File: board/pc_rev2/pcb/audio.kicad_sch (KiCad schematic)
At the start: 29 parts, among them J8 GND Pins, J9 Conn_01x05, Q1 2SC1815, Q2 2SA1015, U3 LMV324B

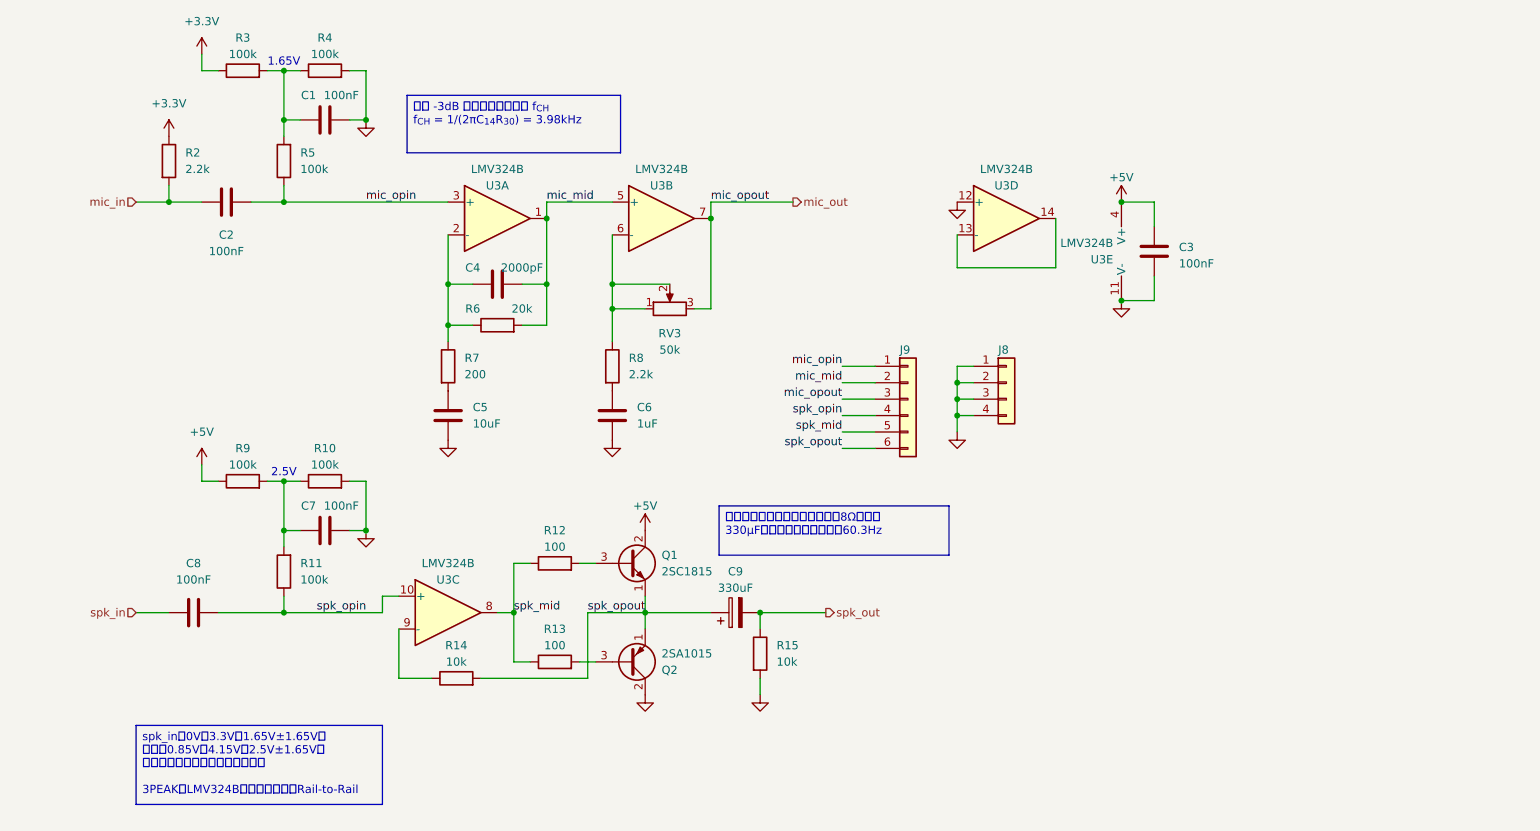
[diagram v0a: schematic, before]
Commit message: MSMP-IFを追加、スピーカ出力をOFFにする仕組みを追加（WIP）
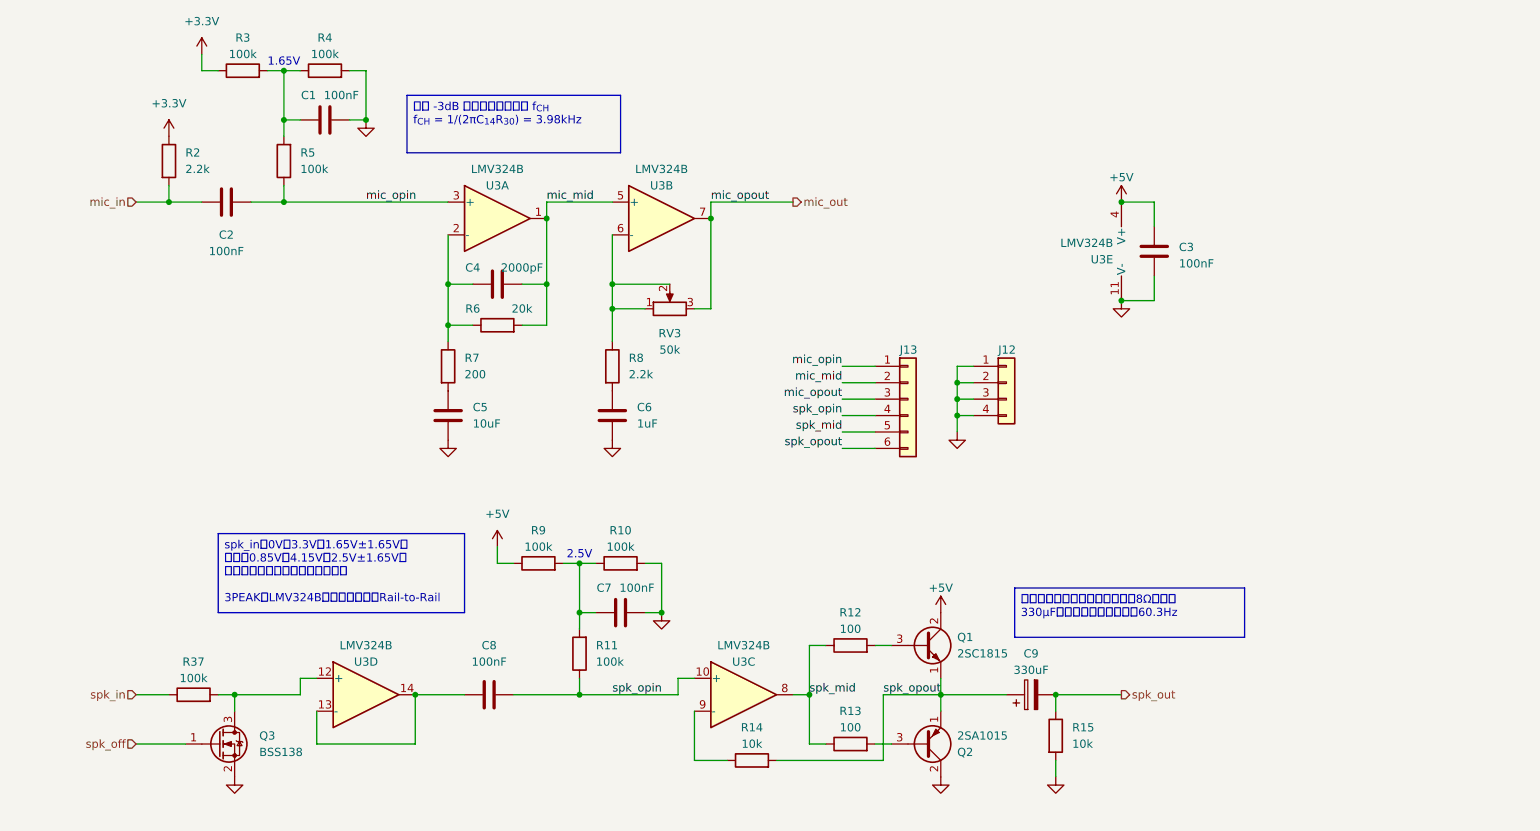
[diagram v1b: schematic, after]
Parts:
- added Q3: BSS138, Package_TO_SOT_SMD:SOT-23_Handsoldering, symbol Device:Q_NMOS_GSD
- added R37: 100k, Resistor_SMD:R_0603_1608Metric_Pad0.98x0.95mm_HandSolder, symbol Device:R
- renumbered J8 to J12, J9 to J13
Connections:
- net GND: now also Q3.2 (S); no longer U3.12 (+)
- net spk_in: now also R37.1; no longer C8.1
- net at U3.13 (-), U3.14: now also C8.1
- new net: Q3.3 (D), R37.2, U3.12 (+)
- new net spk_off: Q3.1 (G)
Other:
- moved on the sheet: C7, C8, C9, Q1, Q2, R10, R11, R12, R13, R14, R15, R9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

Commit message: ADCの8ch化＆スピーカーミュートの仕組み変更
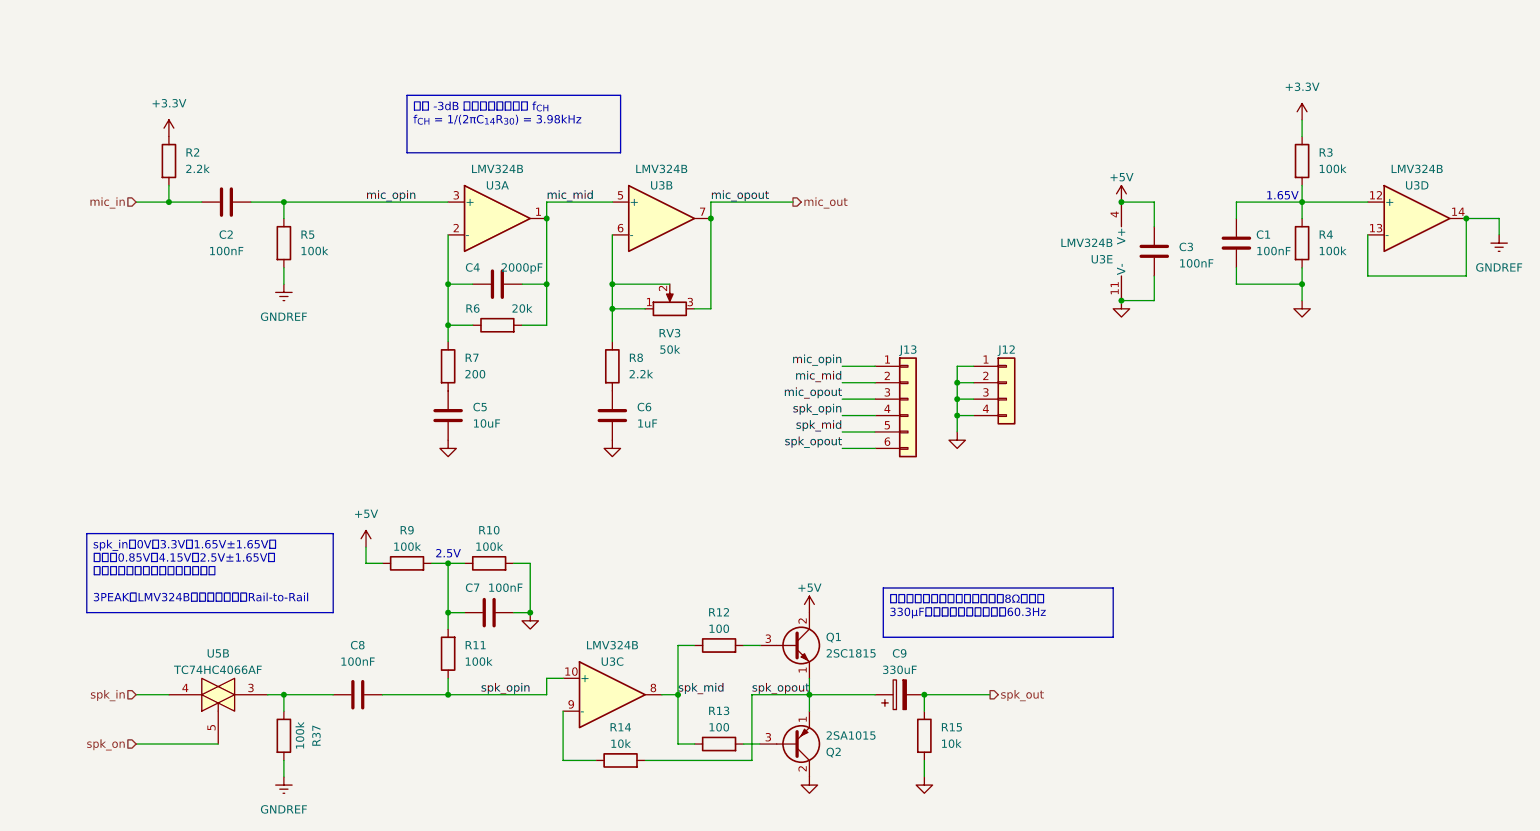
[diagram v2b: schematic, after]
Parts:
- removed Q3: BSS138, Package_TO_SOT_SMD:SOT-23_Handsoldering, symbol Device:Q_NMOS_GSD
- added U5: TC74HC4066AF, Package_SO:SO-14_5.3x10.2mm_P1.27mm, symbol 4xxx:4066
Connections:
- net spk_in: now also U5.4; no longer R37.1
- net at C1.1, R3.2, R4.1: now also U3.12 (+); no longer R5.2
- net GNDREF: now reaches R37.2
- net GNDREF: now also R5.2, U3.13 (-), U3.14; no longer U3.12 (+)
- new net: C8.1, R37.1, U5.3
- new net spk_on: U5.5
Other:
- moved on the sheet: C1, C7, C8, C9, Q1, Q2, R10, R11, R12, R13, R14, R15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

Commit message: 諸々改良＆基板デザイン（WIP）
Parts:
- removed Q1: 2SC1815, Package_TO_SOT_THT:TO-92_Inline, symbol Transistor_BJT:2SC1815
- removed Q2: 2SA1015, Package_TO_SOT_THT:TO-92_Inline, symbol Transistor_BJT:2SA1015
- added C17: 100nF, Capacitor_SMD:C_0603_1608Metric_Pad1.08x0.95mm_HandSolder, symbol Device:C
- added D2: BAT54S, Package_TO_SOT_SMD:SOT-23, symbol Diode:BAT54S
- added J17: GND Pins, Connector_PinHeader_2.54mm:PinHeader_1x02_P2.54mm_Vertical, symbol Connector_Generic:Conn_01x02
- added J18: Conn_01x05, Connector_PinHeader_2.54mm:PinHeader_1x03_P2.54mm_Vertical, symbol Connector_Generic:Conn_01x03
- added J19: Conn_01x02, Connector_PinHeader_2.54mm:PinHeader_1x02_P2.54mm_Vertical, symbol Connector_Generic:Conn_01x02
- added Q1: BC817BPN, Package_TO_SOT_SMD:SOT-457T, symbol Transistor_BJT:Q_Dual_NPN_PNP_E1B1C2E2B2C1
- added R38: 10k, Resistor_SMD:R_0603_1608Metric_Pad0.98x0.95mm_HandSolder, symbol Device:R
- C9: value 330uF -> 470uF; footprint Capacitor_THT:CP_Radial_D6.3mm_P2.50mm -> Capacitor_THT:CP_Radial_D8.0mm_P3.50mm
- J12: footprint Connector_PinHeader_2.54mm:PinHeader_1x04_P2.54mm_Vertical -> Connector_PinHeader_2.54mm:PinHeader_1x02_P2.54mm_Vertical; symbol Connector_Generic:Conn_01x04 -> Connector_Generic:Conn_01x02
- J13: value Conn_01x05 -> Conn_01x02; footprint Connector_PinHeader_2.54mm:PinHeader_1x06_P2.54mm_Vertical -> Connector_PinHeader_2.54mm:PinHeader_1x02_P2.54mm_Vertical; symbol Connector_Generic:Conn_01x06 -> Connector_Generic:Conn_01x02
- R12, R13: value 100 -> 33
- RV3: footprint Potentiometer_SMD:Potentiometer_Bourns_TC33X_Vertical -> uchan:Potentiometer_Suntan_TSR-3386K_Vertical; Manufacturer (none) -> SUNTAN; Manufacturer PN (none) -> TSR-3386K-EY5-503TR
- U3: Manufacturer (none) -> 3PEAK; Manufacturer PN (none) -> LMV324B-TR
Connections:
- net +3.3V: now also D2.2 (K)
- net +5V: now also C17.2, Q1.6 (C1)
- net GND: now also C17.1, D2.1 (A), J17.1 (Pin_1), J17.2 (Pin_2), J19.2 (Pin_2), Q1.3 (C2); no longer J12.3 (Pin_3), J12.4 (Pin_4)
- net GNDREF: now also U3.1, U3.2 (-); no longer U3.13 (-), U3.14
- net mic_mid: now also U3.10 (+), U3.14; no longer U3.1, U3.5 (+)
- net mic_opin: now also U3.12 (+); no longer U3.3 (+)
- net mic_out: now also D2.3 (COM), J19.1 (Pin_1), R38.2; no longer J13.3 (Pin_3), RV3.3, U3.7
- net spk_in: now also U5.1; no longer U5.4
- net spk_mid: now also U3.7, J18.2 (Pin_2); no longer J13.5 (Pin_5), U3.8
- net spk_on: now also U5.13; no longer U5.5
- net spk_opin: now also U3.5 (+), J18.1 (Pin_1); no longer J13.4 (Pin_4), U3.10 (+)
- net spk_opout: now also J18.3 (Pin_3), Q1.1 (E1), Q1.4 (E2); no longer J13.6 (Pin_6)
- net at C4.1, R6.1, R7.1: now also U3.13 (-); no longer U3.2 (-)
- net at C1.1, R3.2, R4.1: now also U3.3 (+); no longer U3.12 (+)
- net at R8.1, RV3.1, RV3.2: now also U3.9 (-); no longer U3.6 (-)
- net at R12.2: now also Q1.2 (B1)
- net at R13.2: now also Q1.5 (B2)
- net at R14.1: now also U3.6 (-); no longer U3.9 (-)
- net at C8.1, R37.1: now also U5.2; no longer U5.3
- new net: R38.1, RV3.3, U3.8

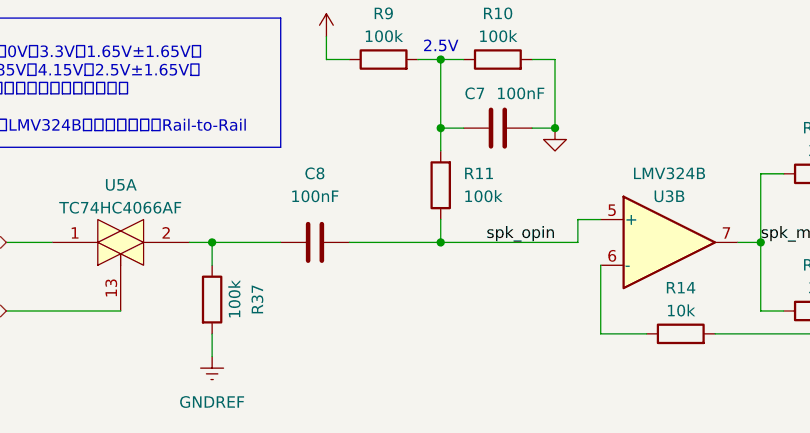
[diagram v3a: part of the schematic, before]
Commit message: ポップノイズ防止用コンデンサ追加＆シルク微修正
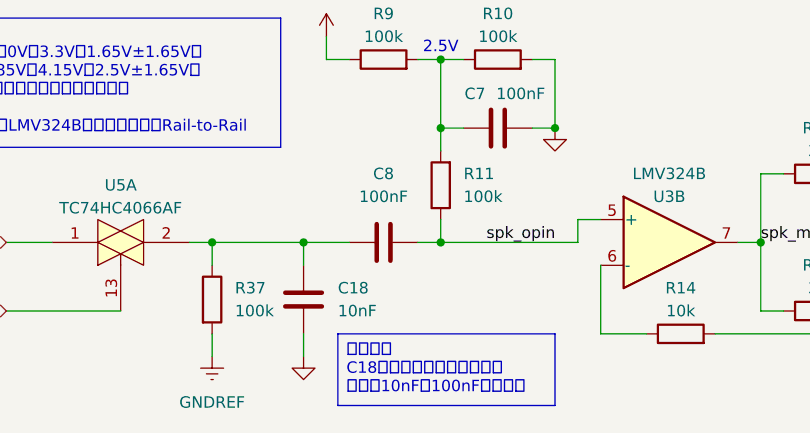
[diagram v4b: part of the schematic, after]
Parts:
- added C18: 10nF, Capacitor_SMD:C_0603_1608Metric_Pad1.08x0.95mm_HandSolder, symbol Device:C
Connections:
- net GND: now also C18.2
- net at C8.1, R37.1, U5.2: now also C18.1
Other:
- moved on the sheet: C8

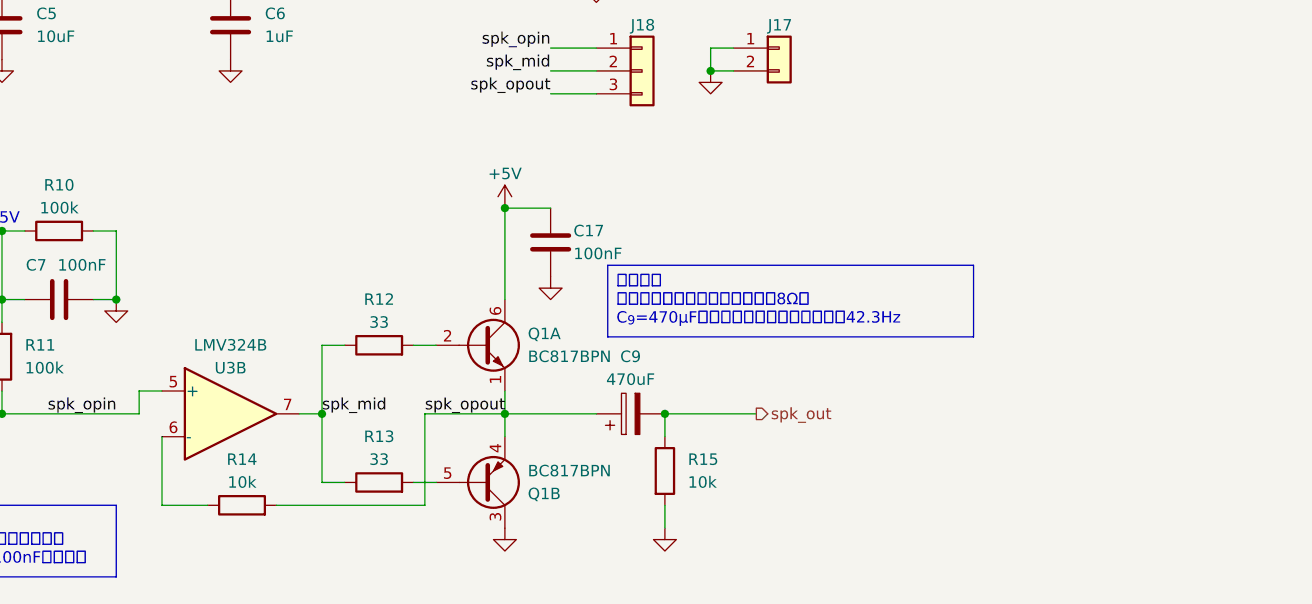
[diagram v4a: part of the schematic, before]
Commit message: オペアンプ入力保護抵抗を追加
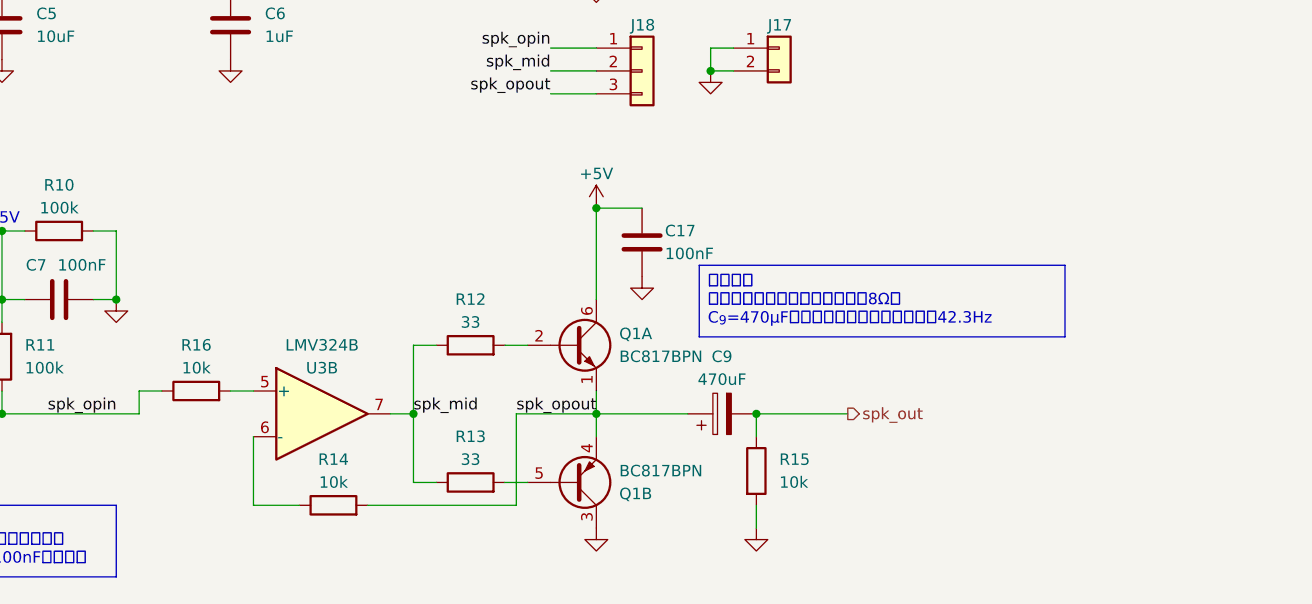
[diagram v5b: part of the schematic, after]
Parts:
- added R16: 10k, Resistor_SMD:R_0603_1608Metric_Pad0.98x0.95mm_HandSolder, symbol Device:R
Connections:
- net spk_opin: now also R16.1; no longer U3.5 (+)
- new net: R16.2, U3.5 (+)
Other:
- moved on the sheet: C17, C9, Q1A, Q1B, R12, R13, R14, R15, U3B
